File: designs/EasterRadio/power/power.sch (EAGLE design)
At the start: 24 parts, among them IC1 MCP73832T-2ACI_OT, IC2 TPS62160DGKR, IC3 DMP1045U-7, J1 10118192-0001LF, J2 S2B-PH-SM4

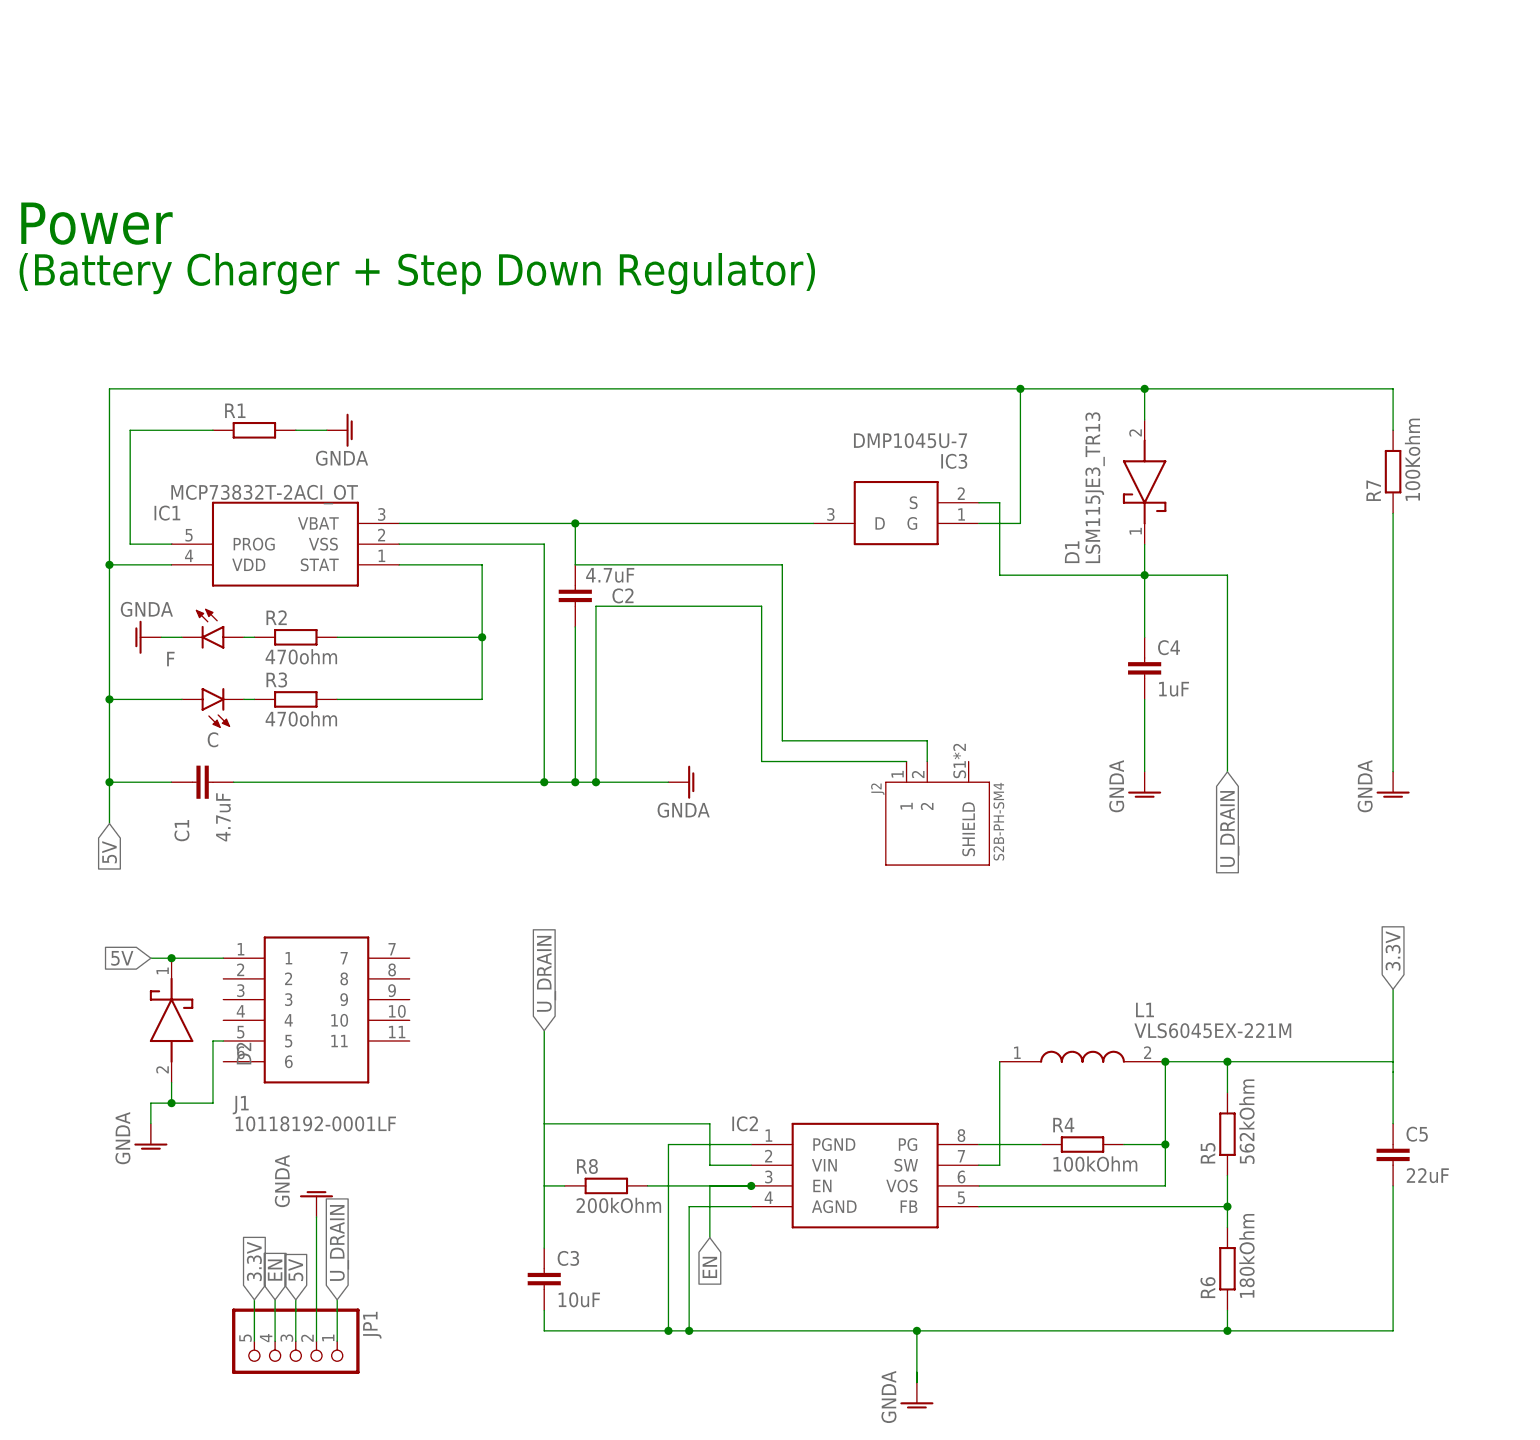
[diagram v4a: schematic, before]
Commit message: added final revisions to amplifier power radio ic and control pcbs
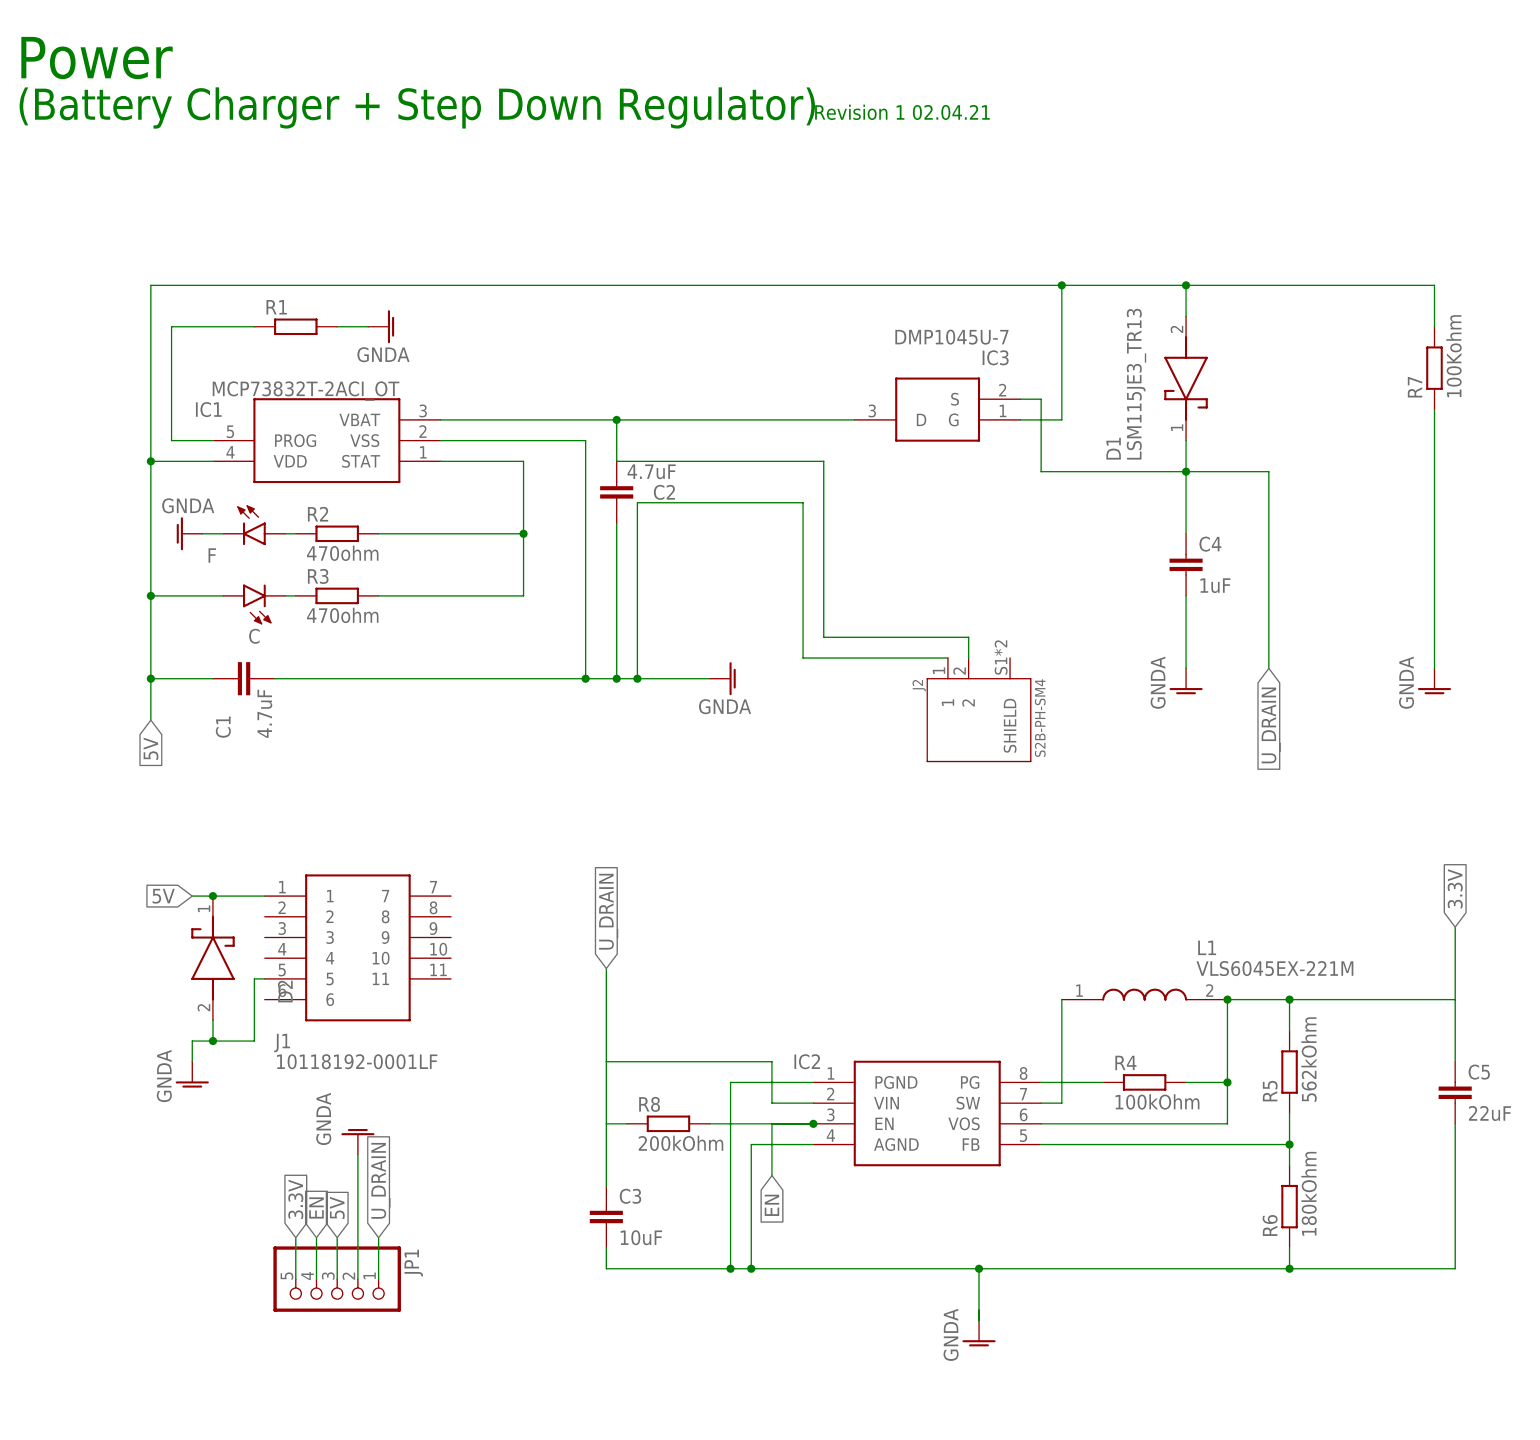
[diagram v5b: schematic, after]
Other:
- note added: "Revision 1 02.04.21"
- note removed: "Mico SD für Spannung"
- note removed: "Step down to 3.3V Converter"
- moved on the sheet: C, C1, C2, C3, C4, C5, D1, D2, F, IC1, IC2, IC3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
